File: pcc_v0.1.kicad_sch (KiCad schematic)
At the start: 62 parts, among them J2 Conn_01x04_Socket, J3 Conn_01x02_Socket, J4 Conn_02x14_Counter_Clockwise, J6 Conn_01x04_Socket, J7 Conn_01x04_Socket, J8 Conn_01x02_Socket, K1 G9KB-1A_DC12, K2 DBR71210, K3 PCN-112D3MHZ_000, U2 4N35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

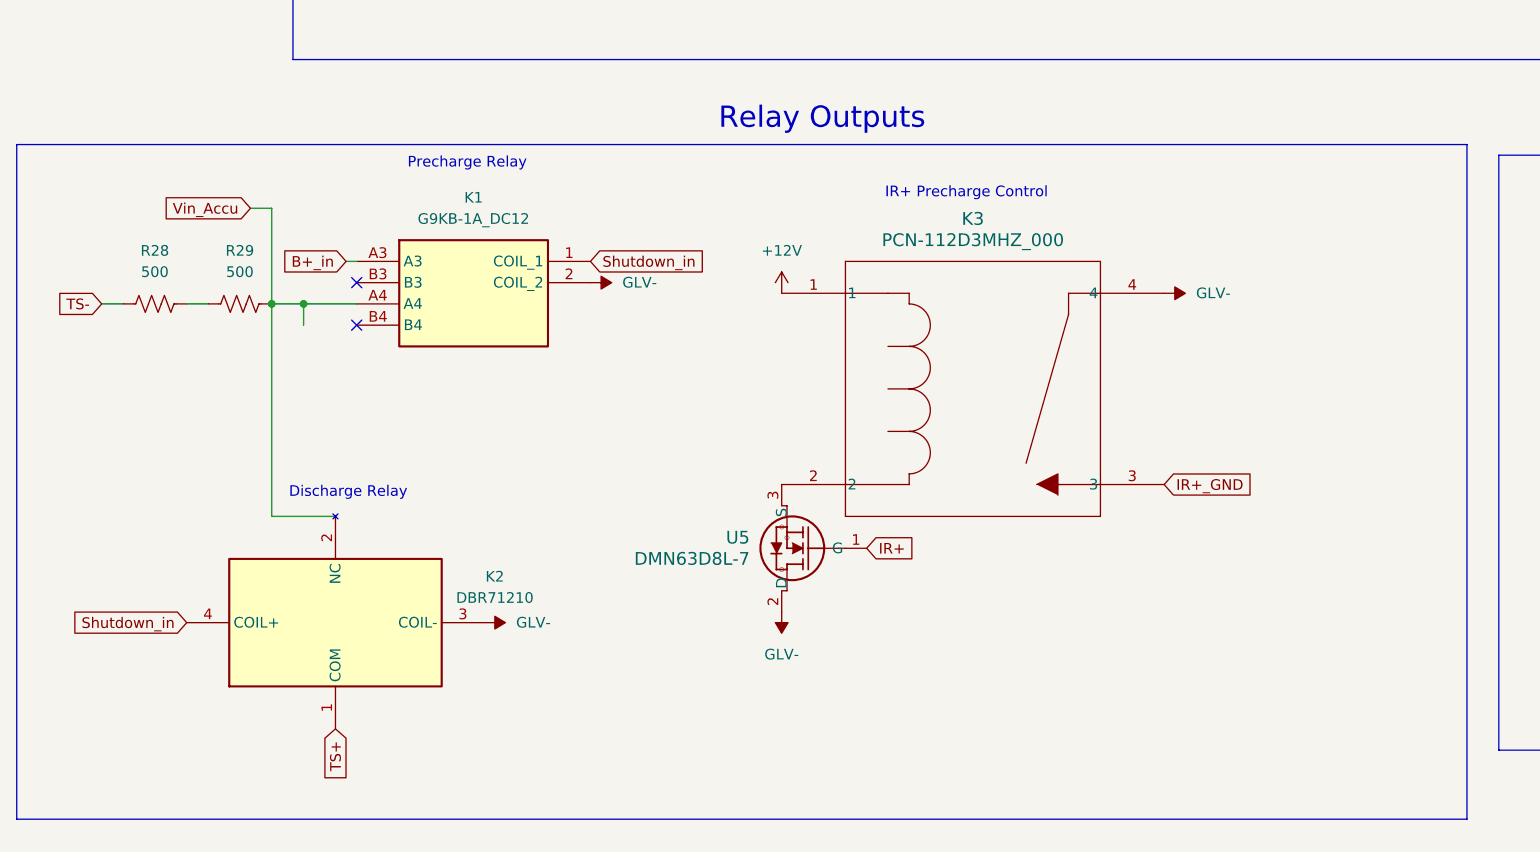
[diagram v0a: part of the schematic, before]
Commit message: made custom footprint for relay. need to measure actual size
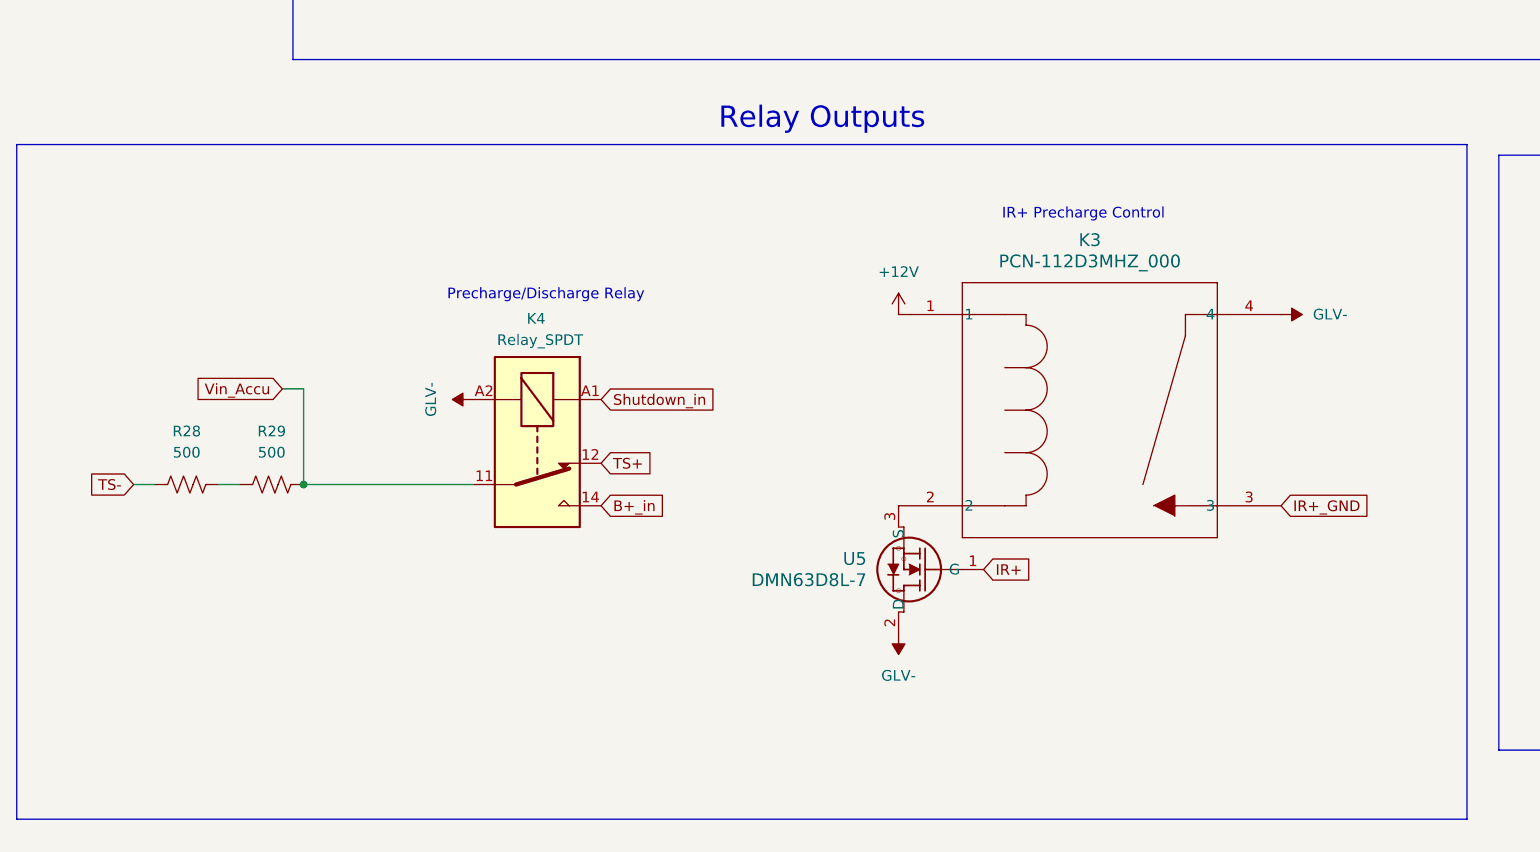
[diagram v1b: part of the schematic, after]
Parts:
- removed K1: G9KB-1A_DC12, precharge relay 2:G9KB1ADC12, symbol G9KB-1A_DC12:G9KB-1A_DC12
- removed K2: DBR71210, discharge relay:DBR71210, symbol DBR71210:DBR71210
- added K4: Relay_SPDT, Relay_THT:Precharge_Discharge_Relay, symbol Relay:Relay_SPDT
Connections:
- net B+_in: now also K4.14
- net GLV-: now also K4.A2
- net Shutdown_in: now also K4.A1
- net TS+: now also K4.12
- net Vin_Accu: now also K4.11
- no-connect marks 70 -> 68
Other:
- note added: "Precharge/Discharge Relay"
- note removed: "Discharge Relay"
- note removed: "Precharge Relay"
- moved on the sheet: K3, R28, R29, U5

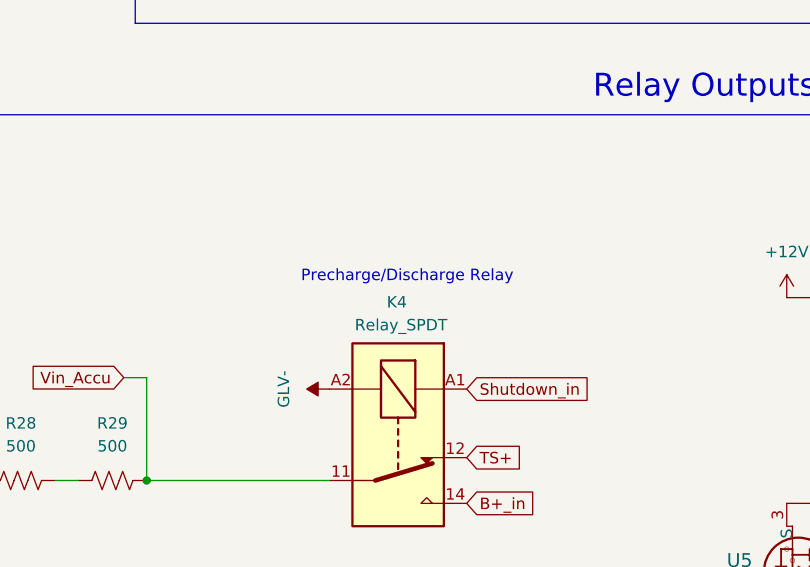
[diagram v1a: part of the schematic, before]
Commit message: corrected relay footprint, added flyback diode
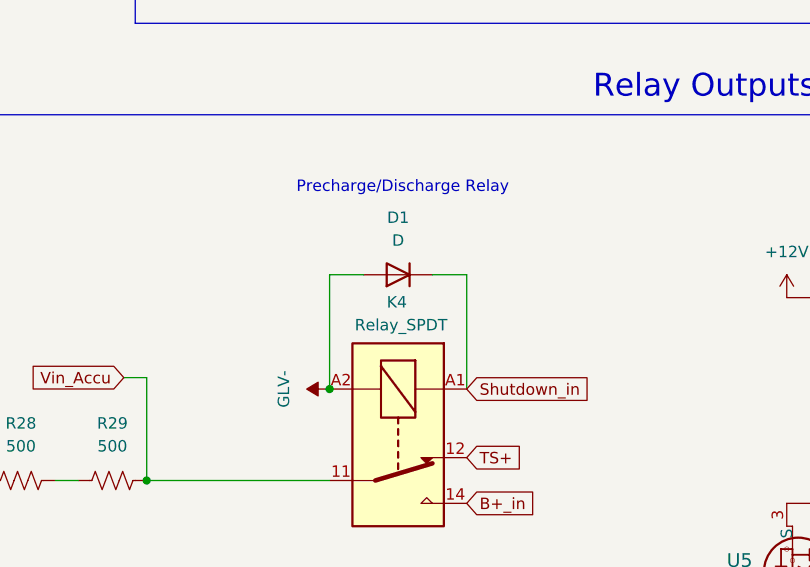
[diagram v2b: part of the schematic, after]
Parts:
- added D1: D, Diode_SMD:D_0805_2012Metric, symbol Device:D
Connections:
- net GLV-: now also D1.2 (A)
- net Shutdown_in: now also D1.1 (K)
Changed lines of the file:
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@@
 	)
 	(junction
+		(at 69.85 189.23)
+		(diameter 0)
+		(color 0 0 0 0)
+	)
+	(junction
 		(at 330.2 115.57)
 		(diameter 0)
@@
 	(wire
 		(pts
+			(xy 85.09 176.53) (xy 85.09 189.23)
+		)
+		(stroke
+			(width 0)
+			(type default)
+		)
+	)
+	(wire
+		(pts
 			(xy 173.99 58.42) (xy 173.99 62.23)
 		)
@@
 	(wire
 		(pts
+			(xy 69.85 176.53) (xy 73.66 176.53)
+		)
+		(stroke
+			(width 0)
+			(type default)
+		)
+	)
+	(wire
+		(pts
 			(xy 355.6 129.54) (xy 358.14 129.54)
 		)
@@
 	(wire
 		(pts
+			(xy 81.28 176.53) (xy 85.09 176.53)
+		)
+		(stroke
+			(width 0)
+			(type default)
+		)
+	)
+	(wire
+		(pts
 			(xy 351.79 99.06) (xy 355.6 99.06)
 		)
@@
 	(wire
 		(pts
+			(xy 69.85 189.23) (xy 69.85 176.53)
+		)
+		(stroke
+			(width 0)
+			(type default)
+		)
+	)
+	(wire
+		(pts
 			(xy 355.6 64.77) (xy 358.14 64.77)
 		)
@@
 	(text "Precharge/Discharge Relay"
 		(exclude_from_sim no)
-		(at 78.486 176.784 0)
+		(at 77.978 166.878 0)
 		(effects
 			(font
@@
 					(unit 1)
 				)
+			)
+		)
+	)
+	(symbol
+		(lib_id "Device:D")
+		(at 77.47 176.53 180)
+		(unit 1)
+		(exclude_from_sim no)
+		(in_bom yes)
+		(on_board yes)
+		(dnp no)
+		(fields_autoplaced yes)
+		(property "Reference" "D1"
+			(at 77.47 170.18 0)
+			(effects
+				(font
+					(size 1.27 1.27)
+				)
+			)
+		)
+		(property "Value" "D"
+			(at 77.47 172.72 0)
+			(effects
+				(font
+					(size 1.27 1.27)
+				)
+			)
+		)
+		(property "Footprint" "Diode_SMD:D_0805_2012Metric"
+			(at 77.47 176.53 0)
+			(effects
+				(font
+					(size 1.27 1.27)
+				)
+				(hide yes)
+			)
+		)
+		(property "Datasheet" "~"
+			(at 77.47 176.53 0)
+			(effects
+				(font
+					(size 1.27 1.27)
+				)
+				(hide yes)
+			)
+		)
+		(property "Description" "Diode"
+			(at 77.47 176.53 0)
+			(effects
+				(font
+					(size 1.27 1.27)
+				)
+				(hide yes)
+			)
+		)
+		(property "Sim.Device" "D"
+			(at 77.47 176.53 0)
+			(effects
+				(font
+					(size 1.27 1.27)
+				)
+				(hide yes)
+			)
+		)
+		(property "Sim.Pins" "1=K 2=A"
+			(at 77.47 176.53 0)
+			(effects
+				(font
+					(size 1.27 1.27)
+				)
+				(hide yes)
+			)
+		)
+		(pin "1"
+		)
+		(pin "2"
+		)
+		(instances
+			(project ""
+				(path "/cd50b4df-2796-417a-bb78-7e5b371bc4af"
+					(reference "D1")
+					(unit 1)
+				)

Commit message: updated schem
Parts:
- D1: footprint Diode_SMD:D_0805_2012Metric -> Diode_THT:D_5KPW_P7.62mm_Vertical_AnodeUp
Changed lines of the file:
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@@
 			)
 		)
-		(property "Footprint" "Diode_SMD:D_0805_2012Metric"
+		(property "Footprint" "Diode_THT:D_5KPW_P7.62mm_Vertical_AnodeUp"
 			(at 77.47 176.53 0)
 			(effects

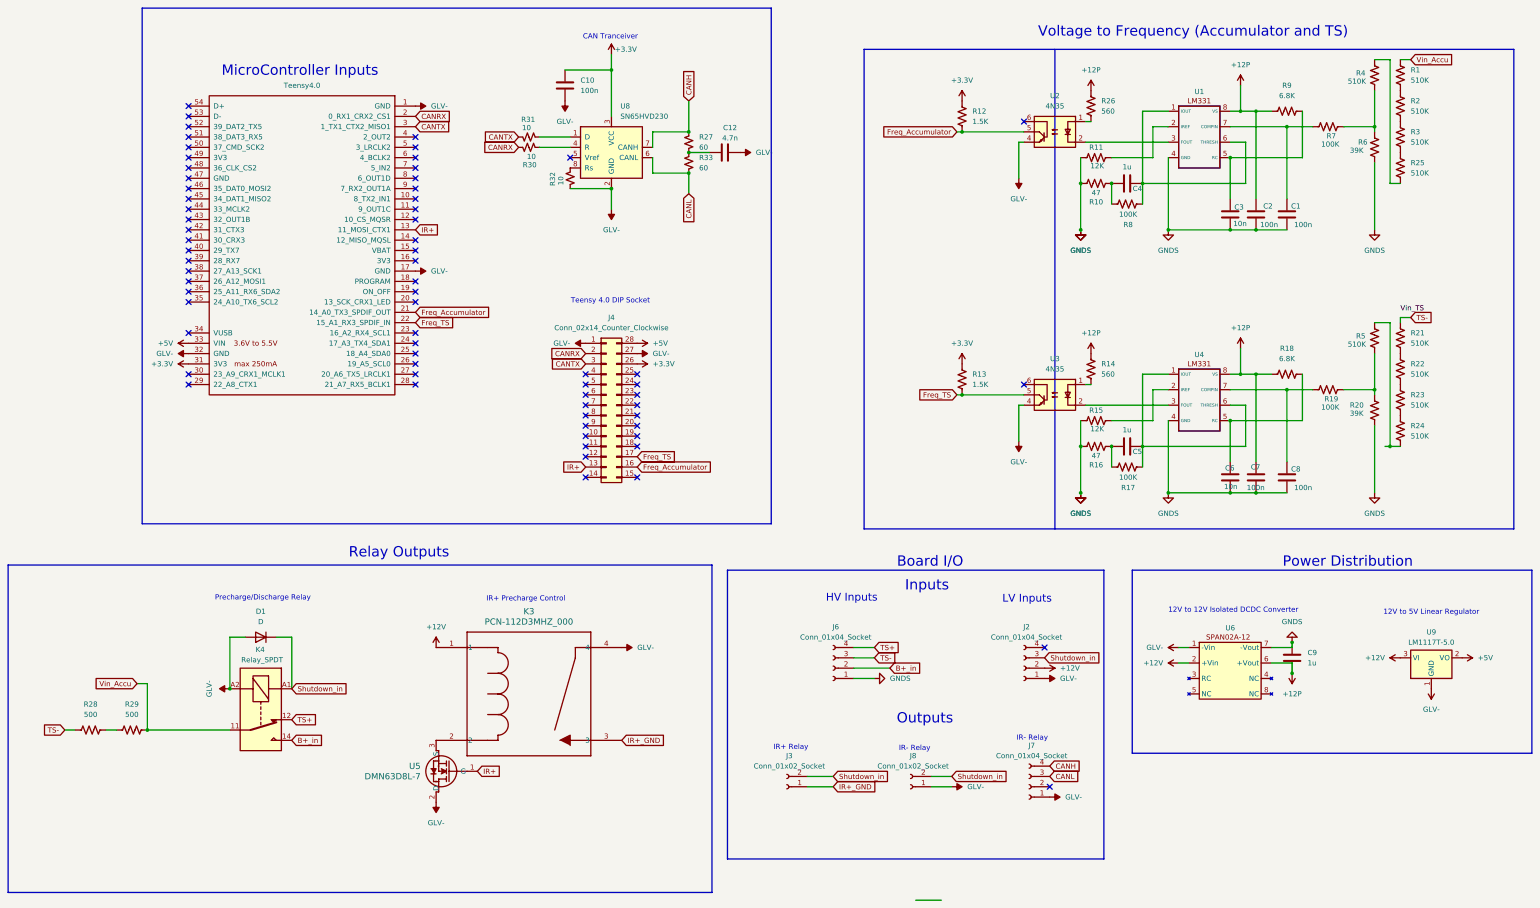
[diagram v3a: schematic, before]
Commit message: made changes based on picture of working breadboard
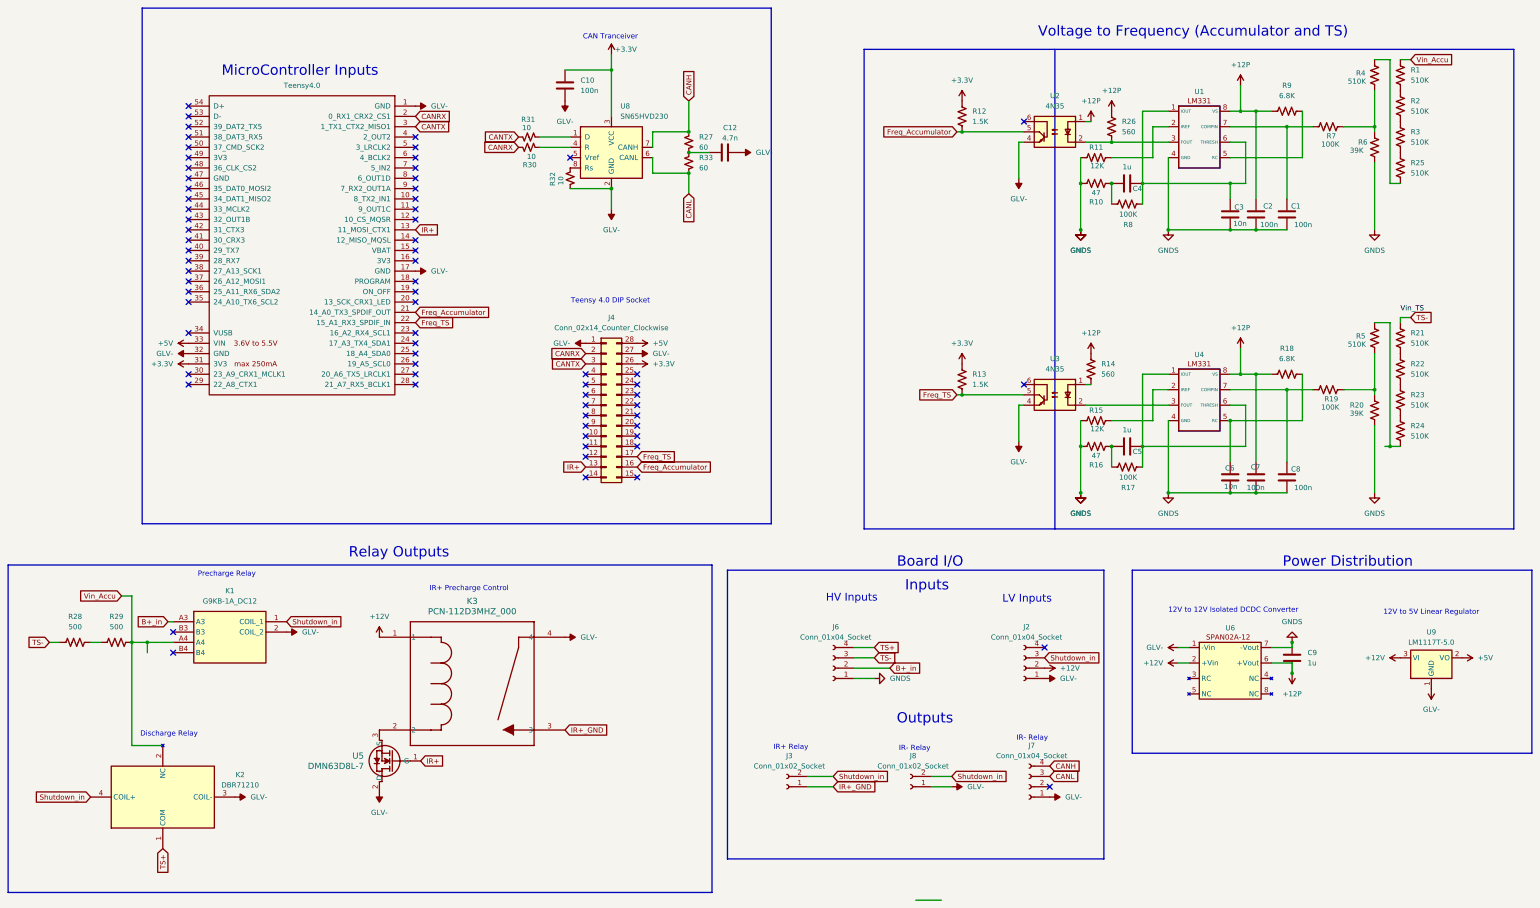
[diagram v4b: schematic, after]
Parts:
- removed D1: D, Diode_THT:D_5KPW_P7.62mm_Vertical_AnodeUp, symbol Device:D
- removed K4: Relay_SPDT, Relay_THT:Precharge_Discharge_Relay, symbol Relay:Relay_SPDT
- added K1: G9KB-1A_DC12, precharge relay 2:G9KB1ADC12, symbol G9KB-1A_DC12:G9KB-1A_DC12
- added K2: DBR71210, discharge relay:DBR71210, symbol DBR71210:DBR71210
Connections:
- net +12P: now also U2.1
- net B+_in: now also K1.A3
- net GLV-: now also K1.2 (COIL_2), K2.3 (COIL-)
- net Shutdown_in: now also K1.1 (COIL_1), K2.4 (COIL+)
- net TS+: now also K2.1 (COM)
- net Vin_Accu: now also K1.A4, K2.2 (NC)
- net at C4.2, R8.2, U1.1 (IOUT)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: now also C3.1
- net at R9.2, U1.5 (RC): no longer C3.1
- net at R26.2: now also U1.3 (FOUT), U2.2; no longer U2.1
- no-connect marks 68 -> 70
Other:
- note added: "Discharge Relay"
- note added: "Precharge Relay"
- note removed: "Precharge/Discharge Relay"
- moved on the sheet: K3, R26, R28, R29, U5
